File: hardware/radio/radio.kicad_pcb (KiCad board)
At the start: 2 copper layers, 75 x 40 mm, 38 parts, among them J1 Header, J2 I2C, Q1 BSD840NH6327XTSA1, SW1 Voltage Selector, U1 Si4706-D50-GM, U2 MIC5504-3.3YM5, Y1 32.786kHz

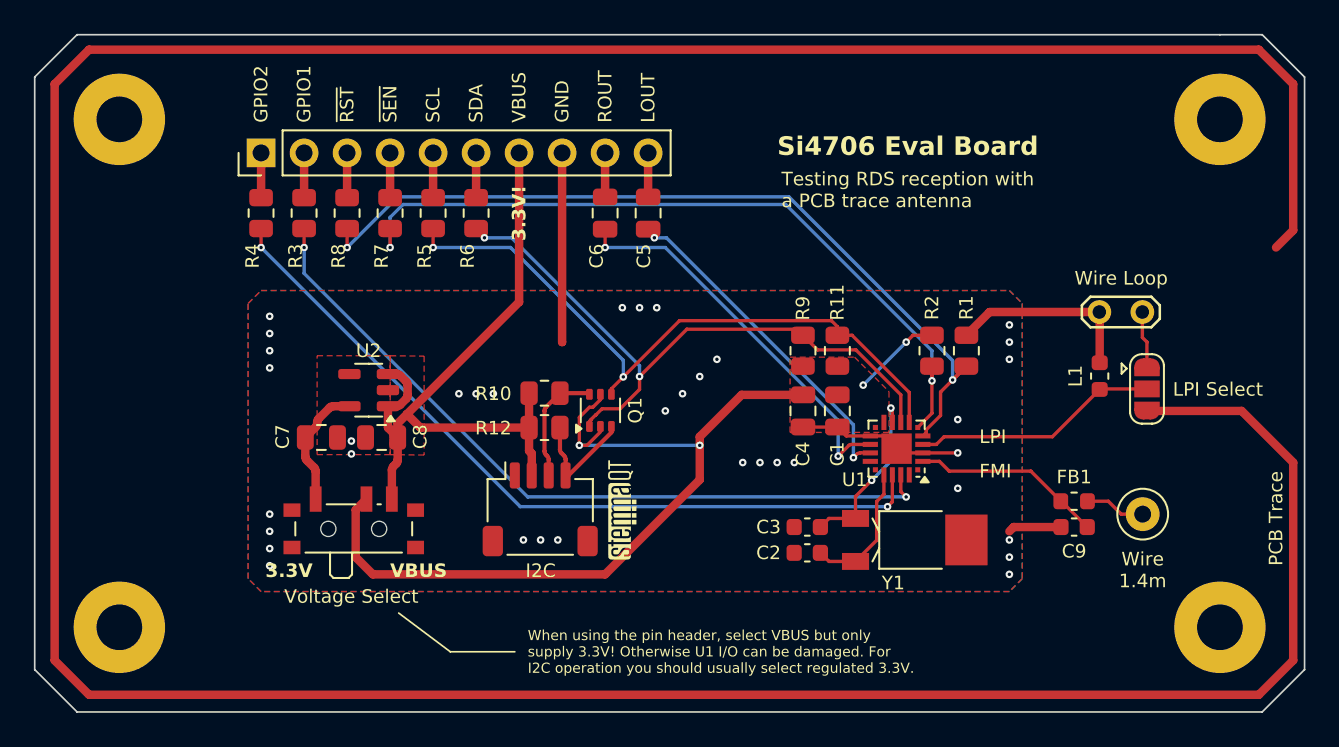
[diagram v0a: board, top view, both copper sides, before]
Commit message: radio: small pcb update, add example firmware to get RDS signal
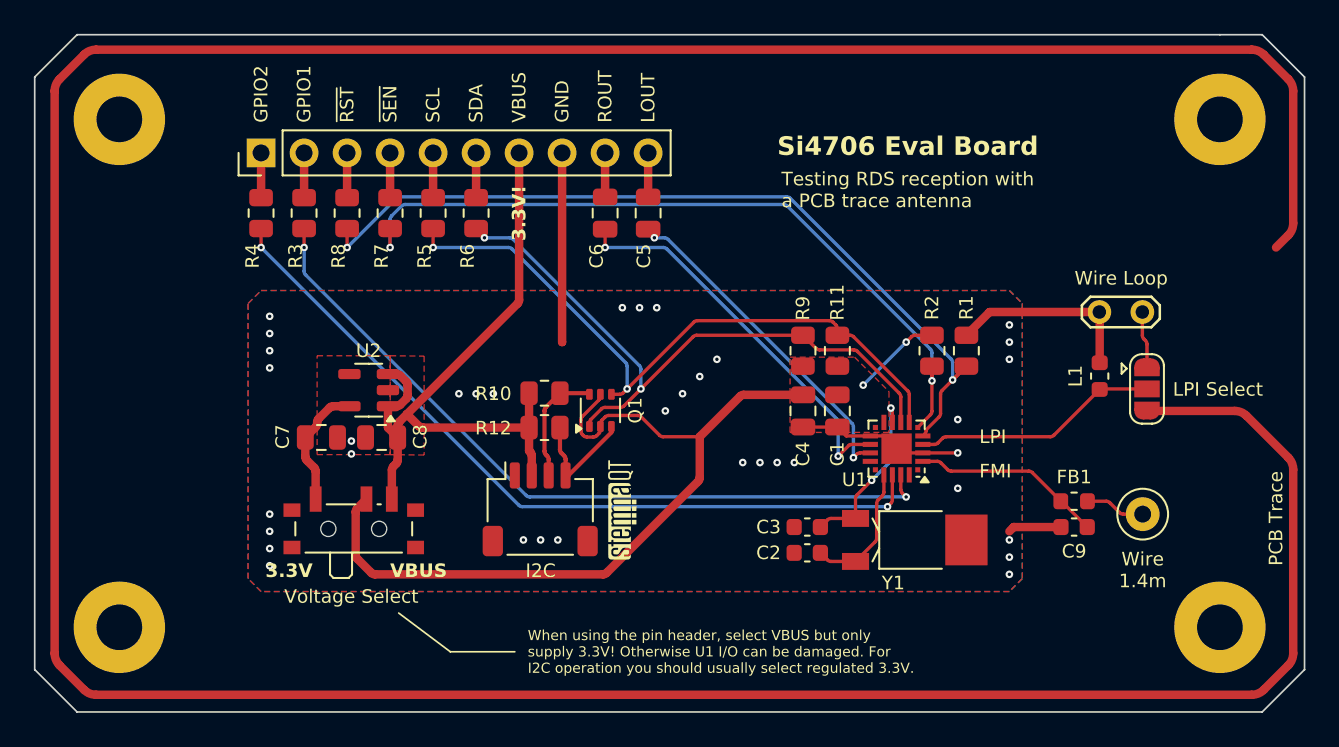
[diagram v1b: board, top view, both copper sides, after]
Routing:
- net VCC: track 54.0 -> 52.7 mm, vias 4 -> 2
- net Net-(JP2-B): track 215.4 -> 214.8 mm
